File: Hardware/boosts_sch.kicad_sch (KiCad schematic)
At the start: 46 parts, among them IC1 AP2205-W5-7, IC2 AP2205-W5-7, IC3 TPS61089RNRR, IC4 TPS61089RNRR

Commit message: updated sensors and other stuff
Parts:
- R102: value 51k -> 49.9k
- R107: value 360k -> 432k
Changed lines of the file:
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@@
 		(on_board yes)
 		(dnp no)
-		(fields_autoplaced yes)
 		(property "Reference" "R102"
-			(at 215.392 30.607 0)
-			(effects
-				(font
-					(size 1.27 1.27)
-				)
-				(justify right)
-			)
-		)
-		(property "Value" "51k"
-			(at 215.392 28.067 0)
-			(effects
-				(font
-					(size 1.27 1.27)
-				)
-				(justify right)
+			(at 212.852 29.464 0)
+			(effects
+				(font
+					(size 1.27 1.27)
+				)
+				(justify left)
+			)
+		)
+		(property "Value" "49.9k"
+			(at 219.71 29.718 0)
+			(effects
+				(font
+					(size 1.27 1.27)
+				)
+				(justify left)
 			)
 		)
@@
 			)
 		)
-		(property "Value" "360k"
+		(property "Value" "432k"
 			(at 224.282 33.782 0)
 			(effects

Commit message: rearranged comps
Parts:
- R97: footprint Resistor_SMD:R_0603_1608Metric -> Resistor_SMD:R_0402_1005Metric
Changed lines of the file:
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@@
 			)
 		)
-		(property "Footprint" "Resistor_SMD:R_0603_1608Metric"
+		(property "Footprint" "Resistor_SMD:R_0402_1005Metric"
 			(at 112.522 40.132 0)
 			(effects

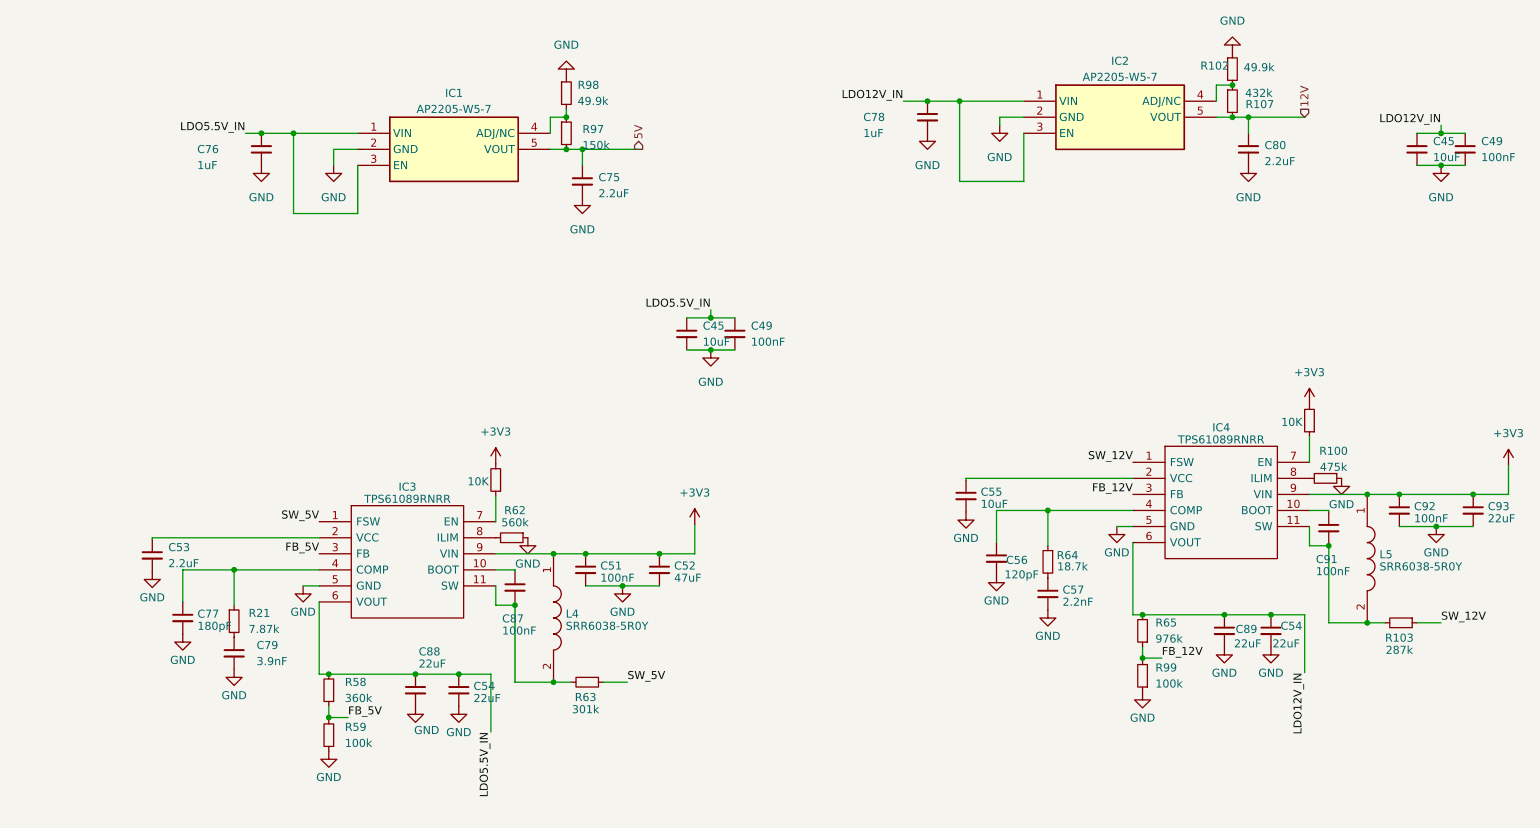
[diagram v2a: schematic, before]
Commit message: Finished Boosts and Sensors
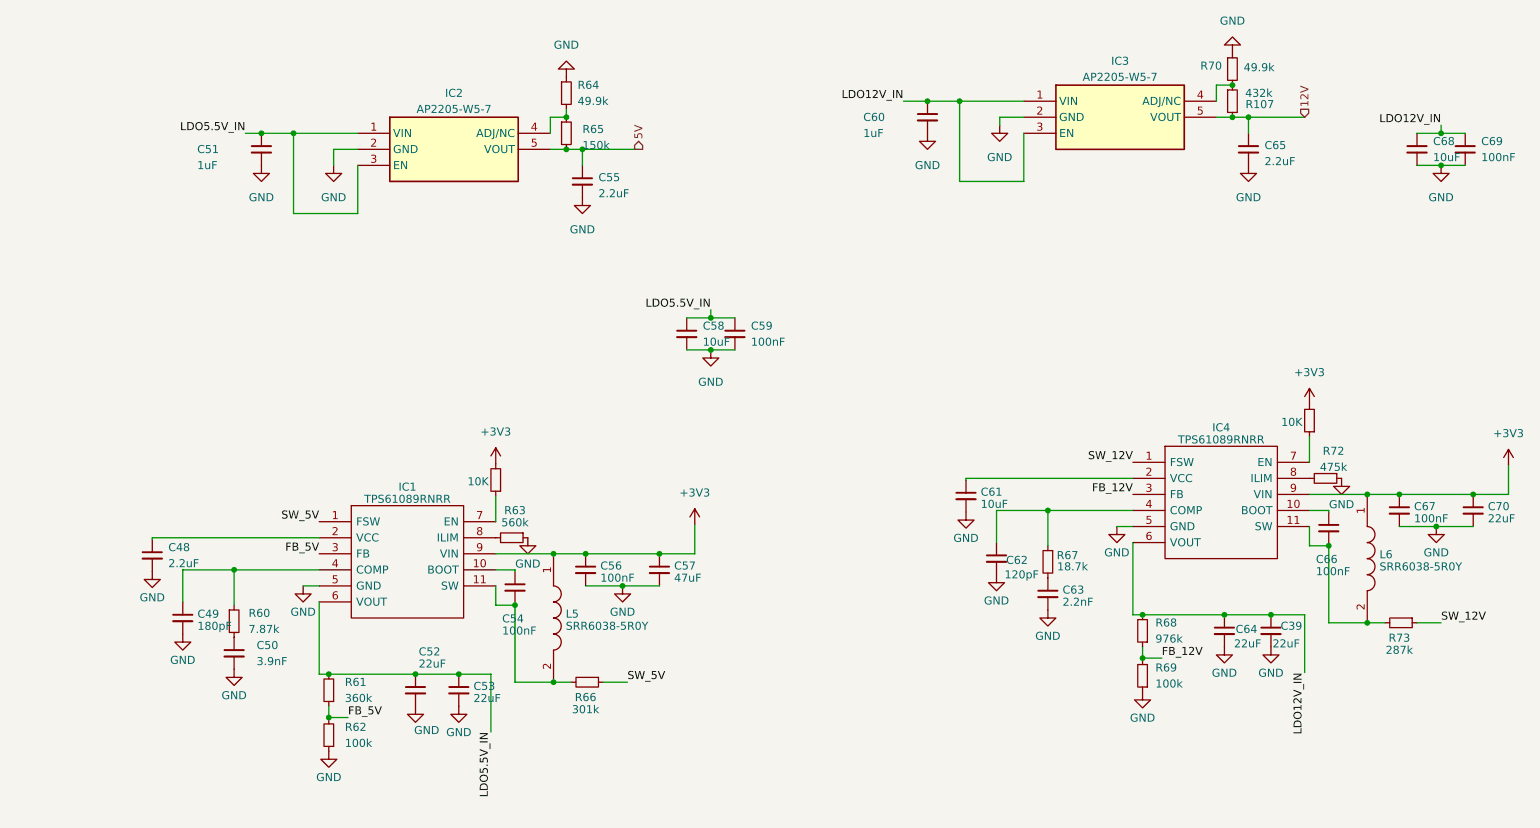
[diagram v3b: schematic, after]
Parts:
- renumbered C54 to C39, C53 to C48, C77 to C49, C79 to C50, C76 to C51, C88 to C52, C54 to C53, C87 to C54, C75 to C55, C51 to C56, C52 to C57, C45 to C58, C49 to C59, C78 to C60, C55 to C61, C56 to C62, C57 to C63, C89 to C64, C80 to C65, C91 to C66, C92 to C67, C45 to C68, C49 to C69, C93 to C70, IC3 to IC1, IC1 to IC2, IC2 to IC3, L4 to L5, L5 to L6, R62 to R10, R21 to R60, R58 to R61, R59 to R62, R62 to R63, R98 to R64, R97 to R65, R63 to R66, R64 to R67, R65 to R68, R99 to R69, R102 to R70, R100 to R72, R103 to R73, R62 to R9

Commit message: v2 Ready for Review
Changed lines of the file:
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@@
 		(on_board yes)
 		(dnp no)
-		(fields_autoplaced yes)
 		(property "Reference" "R65"
 			(at 115.062 39.497 0)
@@
 		)
 		(property "Value" "150k"
-			(at 115.062 42.037 0)
+			(at 114.99 41.58 0)
 			(effects
 				(font

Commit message: Most Review Changes
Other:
- moved on the sheet: C58, C59
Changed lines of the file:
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@@
 	)
 	(junction
-		(at 135.382 69.342)
+		(at 38.1 38.862)
 		(diameter 0)
 		(color 0 0 0 0)
@@
 	)
 	(junction
-		(at 135.382 74.422)
+		(at 38.1 43.942)
 		(diameter 0)
 		(color 0 0 0 0)
@@
 	(wire
 		(pts
-			(xy 135.382 68.072) (xy 135.382 69.342)
+			(xy 38.1 37.592) (xy 38.1 38.862)
 		)
 		(stroke
@@
 	(wire
 		(pts
-			(xy 135.382 69.342) (xy 139.192 69.342)
+			(xy 38.1 38.862) (xy 41.91 38.862)
 		)
 		(stroke
@@
 	(wire
 		(pts
-			(xy 131.572 74.422) (xy 135.382 74.422)
+			(xy 34.29 43.942) (xy 38.1 43.942)
 		)
 		(stroke
@@
 	(wire
 		(pts
-			(xy 135.382 74.422) (xy 139.192 74.422)
+			(xy 38.1 43.942) (xy 41.91 43.942)
 		)
 		(stroke
@@
 	(wire
 		(pts
-			(xy 131.572 69.342) (xy 135.382 69.342)
+			(xy 34.29 38.862) (xy 38.1 38.862)
 		)
 		(stroke
@@
 	)
 	(label "LDO5.5V_IN"
-		(at 135.382 68.072 180)
+		(at 38.1 37.592 180)
 		(effects
 			(font
@@
 	(symbol
 		(lib_id "Device:C_Small")
-		(at 131.572 71.882 0)
+		(at 34.29 41.402 0)
 		(unit 1)
 		(exclude_from_sim no)
@@
 		(fields_autoplaced yes)
 		(property "Reference" "C58"
-			(at 134.112 70.6182 0)
+			(at 36.83 40.1382 0)
 			(effects
 				(font
@@
 		)
 		(property "Value" "10uF"
-			(at 134.112 73.1582 0)
+			(at 36.83 42.6782 0)
 			(effects
 				(font
@@
 		)
 		(property "Footprint" "Capacitor_SMD:C_0402_1005Metric"
-			(at 131.572 71.882 0)
+			(at 34.29 41.402 0)
 			(effects
 				(font
@@
 		)
 		(property "Datasheet" "~"
-			(at 131.572 71.882 0)
+			(at 34.29 41.402 0)
 			(effects
 				(font
@@
 		)
 		(property "Description" ""
-			(at 131.572 71.882 0)
+			(at 34.29 41.402 0)
 			(effects
 				(font
@@
 		(dnp no)
 		(property "Reference" "C66"
-			(at 231.14 107.553 0)
+			(at 233.68 104.505 0)
 			(effects
 				(font
@@
 		)
 		(property "Value" "100nF"
-			(at 231.14 109.474 0)
+			(at 233.68 106.426 0)
 			(effects
 				(font
@@
 	(symbol
 		(lib_id "Device:C_Small")
-		(at 139.192 71.882 0)
+		(at 41.91 41.402 0)
 		(unit 1)
 		(exclude_from_sim no)
@@
 		(fields_autoplaced yes)
 		(property "Reference" "C59"
-			(at 141.732 70.6182 0)
+			(at 44.45 40.1382 0)
 			(effects
 				(font
@@
 		)
 		(property "Value" "100nF"
-			(at 141.732 73.1582 0)
+			(at 44.45 42.6782 0)
 			(effects
 				(font
@@
 		)
 		(property "Footprint" "Capacitor_SMD:C_0402_1005Metric"
-			(at 139.192 71.882 0)
+			(at 41.91 41.402 0)
 			(effects
 				(font
@@
 		)
 		(property "Datasheet" "~"
-			(at 139.192 71.882 0)
+			(at 41.91 41.402 0)
 			(effects
 				(font
@@
 		)
 		(property "Description" ""
-			(at 139.192 71.882 0)
+			(at 41.91 41.402 0)
 			(effects
 				(font
@@
 	(symbol
 		(lib_id "power:GND")
-		(at 135.382 74.422 0)
+		(at 38.1 43.942 0)
 		(unit 1)
 		(exclude_from_sim no)
@@
 		(fields_autoplaced yes)
 		(property "Reference" "#PWR0127"
-			(at 135.382 80.772 0)
+			(at 38.1 50.292 0)
 			(effects
 				(font
@@
 		)
 		(property "Value" "GND"
-			(at 135.382 79.502 0)
+			(at 38.1 49.022 0)
 			(effects
 				(font
@@
 		)
 		(property "Footprint" ""
-			(at 135.382 74.422 0)
+			(at 38.1 43.942 0)
 			(effects
 				(font
@@
 		)
 		(property "Datasheet" ""
-			(at 135.382 74.422 0)
+			(at 38.1 43.942 0)
 			(effects
 				(font
@@
 		)
 		(property "Description" ""
-			(at 135.382 74.422 0)
+			(at 38.1 43.942 0)
 			(effects
 				(font
@@
 		(on_board yes)
 		(dnp no)
-		(fields_autoplaced yes)
 		(property "Reference" "C53"
-			(at 97.8281 127.6326 0)
+			(at 94.488 122.031 0)
 			(effects
 				(font
@@
 		)
 		(property "Value" "22uF"
-			(at 97.8281 129.5536 0)
+			(at 94.488 123.952 0)
 			(effects
 				(font
@@
 		(dnp no)
 		(property "Reference" "C64"
-			(at 218.44 118.618 0)
+			(at 216.916 112.268 0)
 			(effects
 				(font
@@
 		)
 		(property "Value" "22uF"
-			(at 218.186 120.904 0)
+			(at 216.662 114.554 0)
 			(effects
 				(font
@@
 		(dnp no)
 		(property "Reference" "C54"
-			(at 102.362 116.951 0)
+			(at 105.156 113.792 0)
 			(effects
 				(font
@@
 		)
 		(property "Value" "100nF"
-			(at 102.362 118.872 0)
+			(at 105.156 115.713 0)
 			(effects
 				(font
@@
 		(dnp no)
 		(property "Reference" "C39"
-			(at 225.552 118.11 0)
+			(at 222.758 112.268 0)
 			(effects
 				(font
@@
 		)
 		(property "Value" "22uF"
-			(at 224.282 120.904 0)
+			(at 222.758 114.554 0)
 			(effects
 				(font

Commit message: quick changes before silwood
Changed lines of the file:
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@@
 		(color 0 0 0 0)
+	)
+	(bus_entry
+		(at 215.9 115.57)
+		(size 2.54 2.54)
+		(stroke
+			(width 0)
+			(type default)
+		)
 	)
 	(wire

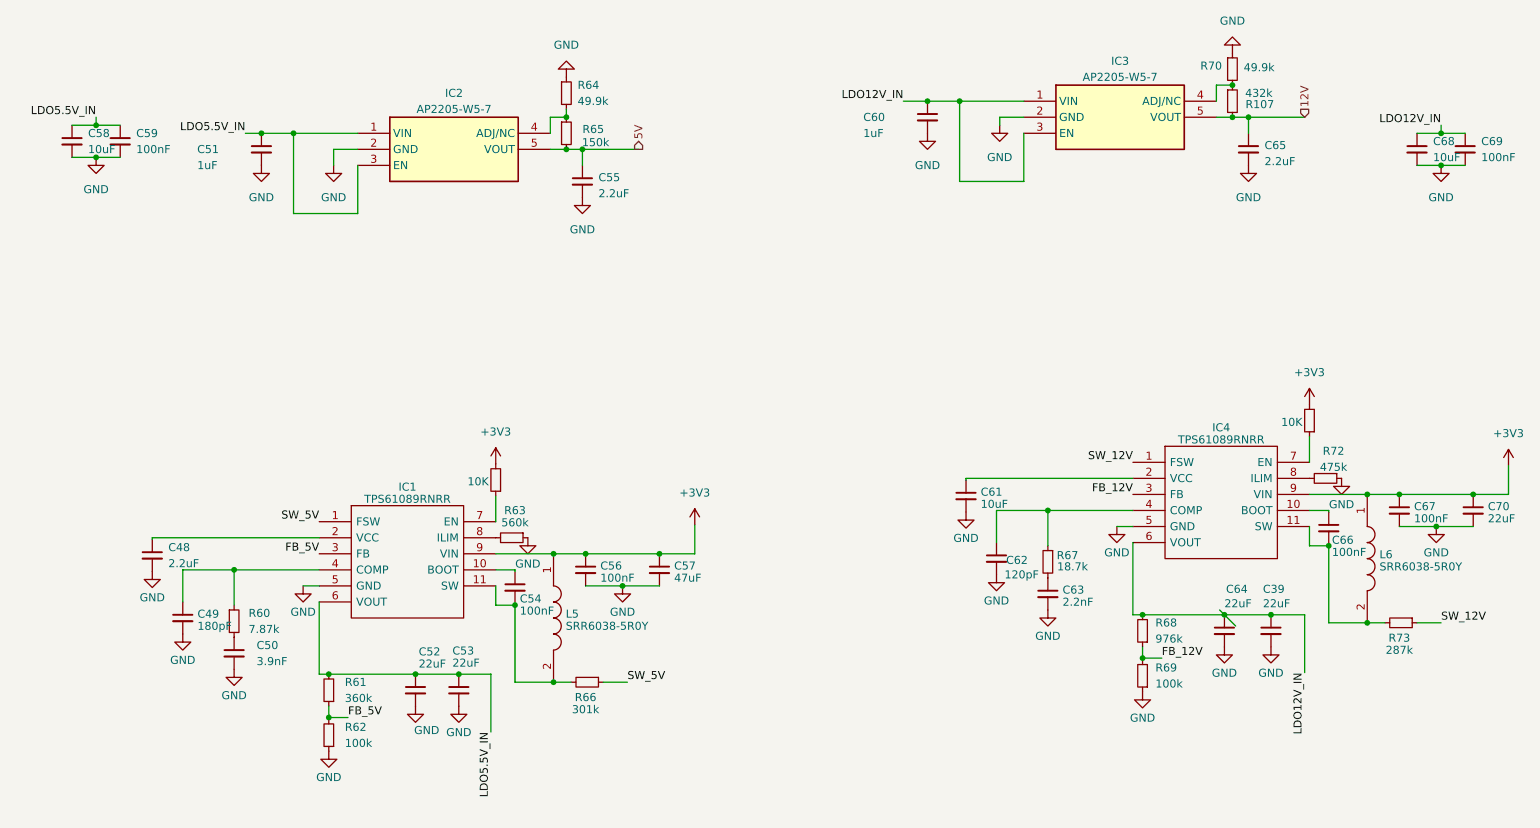
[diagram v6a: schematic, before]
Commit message: schematic reformatting and bom consolidation
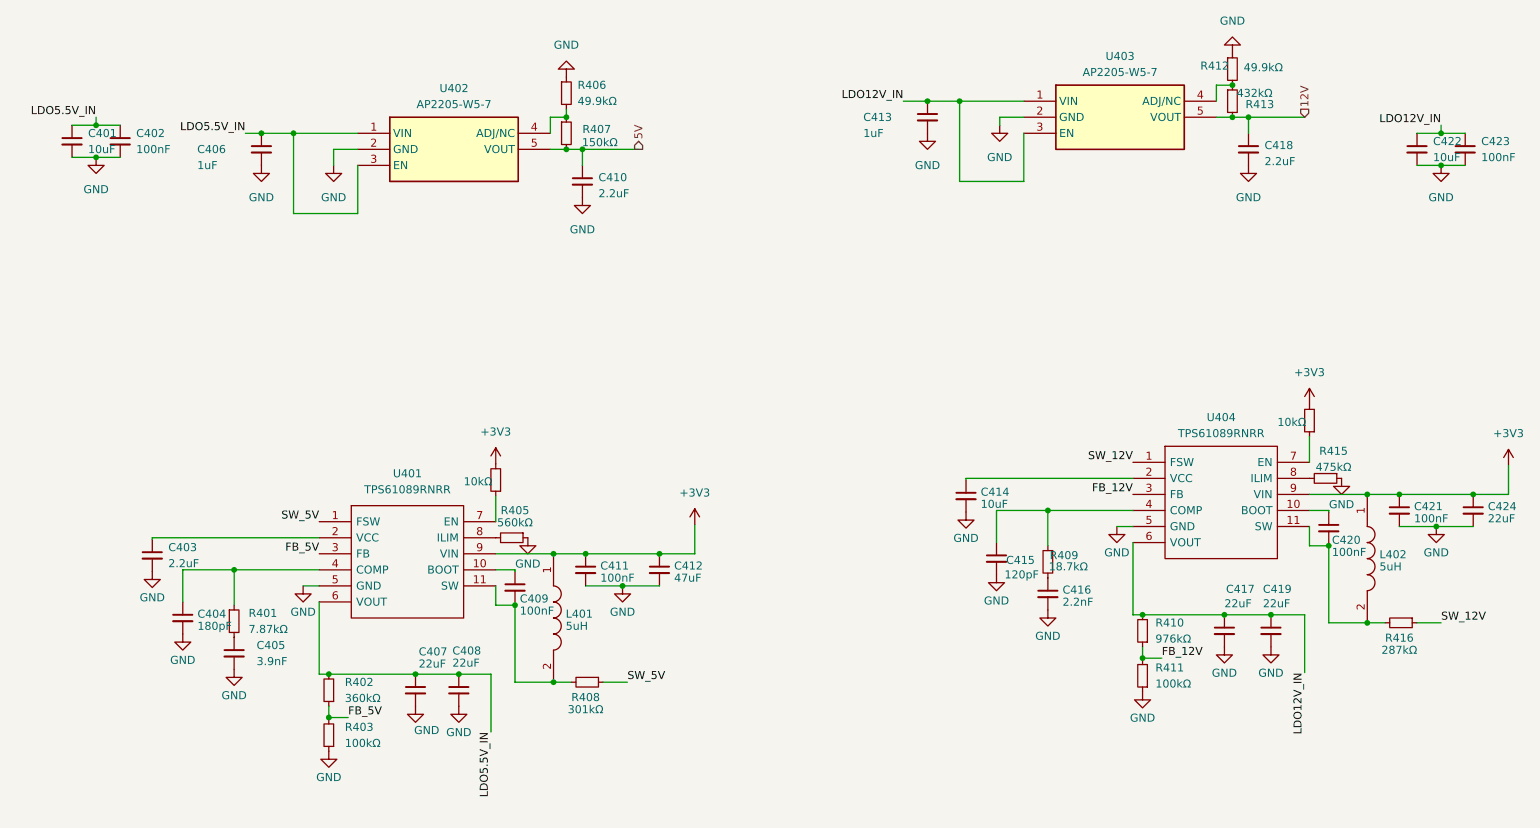
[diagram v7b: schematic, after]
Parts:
- L401: renamed from L5; value SRR6038-5R0Y -> 5uH
- L402: renamed from L6; value SRR6038-5R0Y -> 5uH
- R401: renamed from R60; value 7.87k -> 7.87kΩ
- R402: renamed from R61; value 360k -> 360kΩ
- R403: renamed from R62; value 100k -> 100kΩ
- R404: renamed from R9; value 10K -> 10kΩ
- R405: renamed from R63; value 560k -> 560kΩ
- R406: renamed from R64; value 49.9k -> 49.9kΩ
- R407: renamed from R65; value 150k -> 150kΩ
- R408: renamed from R66; value 301k -> 301kΩ
- R409: renamed from R67; value 18.7k -> 18.7kΩ
- R410: renamed from R68; value 976k -> 976kΩ
- R411: renamed from R69; value 100k -> 100kΩ
- R412: renamed from R70; value 49.9k -> 49.9kΩ
- R413: renamed from R107; value 432k -> 432kΩ
- R414: renamed from R10; value 10K -> 10kΩ
- R415: renamed from R72; value 475k -> 475kΩ
- R416: renamed from R73; value 287k -> 287kΩ
- renumbered C58 to C401, C59 to C402, C48 to C403, C49 to C404, C50 to C405, C51 to C406, C52 to C407, C53 to C408, C54 to C409, C55 to C410, C56 to C411, C57 to C412, C60 to C413, C61 to C414, C62 to C415, C63 to C416, C64 to C417, C65 to C418, C39 to C419, C66 to C420, C67 to C421, C68 to C422, C69 to C423, C70 to C424, IC1 to U401, IC2 to U402, IC3 to U403, IC4 to U404
